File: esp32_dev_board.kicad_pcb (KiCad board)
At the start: 4 copper layers, 0 parts

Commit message: Start layout.
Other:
- board outline added: 100 x 40 mm
- rule via_min_size: 0.4 -> 0.45
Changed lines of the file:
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@@
   (general
     (thickness 1.6)
-    (drawings 0)
+    (drawings 8)
     (tracks 0)
     (zones 0)
@@
     (0 F.Cu signal)
     (1 In1.Cu power)
-    (2 In2.Cu signal)
+    (2 In2.Cu power)
     (31 B.Cu signal)
-    (33 F.Adhes user)
+    (34 B.Paste user)
     (35 F.Paste user)
+    (36 B.SilkS user)
     (37 F.SilkS user)
+    (38 B.Mask user)
     (39 F.Mask user)
     (40 Dwgs.User user)
@@
     (46 B.CrtYd user)
     (47 F.CrtYd user)
+    (48 B.Fab user)
     (49 F.Fab user)
   )
@@
     (via_size 0.8)
     (via_drill 0.4)
-    (via_min_size 0.4)
+    (via_min_size 0.45)
     (via_min_drill 0.3)
     (uvia_size 0.3)
@@
     (uvia_drill 0.1)
   )
+  (gr_line (start 80.2 80.2) (end 80.2 119.8) (layer Margin) (width 0.15))
+  (gr_line (start 179.8 80.2) (end 80.2 80.2) (layer Margin) (width 0.15))
+  (gr_line (start 179.8 119.8) (end 179.8 80.2) (layer Margin) (width 0.15))
+  (gr_line (start 80.2 119.8) (end 179.8 119.8) (layer Margin) (width 0.15))
+  (gr_line (start 80 80) (end 80 120) (layer Edge.Cuts) (width 0.05))
+  (gr_line (start 180 80) (end 80 80) (layer Edge.Cuts) (width 0.05))
+  (gr_line (start 180 120) (end 180 80) (layer Edge.Cuts) (width 0.05))
+  (gr_line (start 80 120) (end 180 120) (layer Edge.Cuts) (width 0.05))
 )

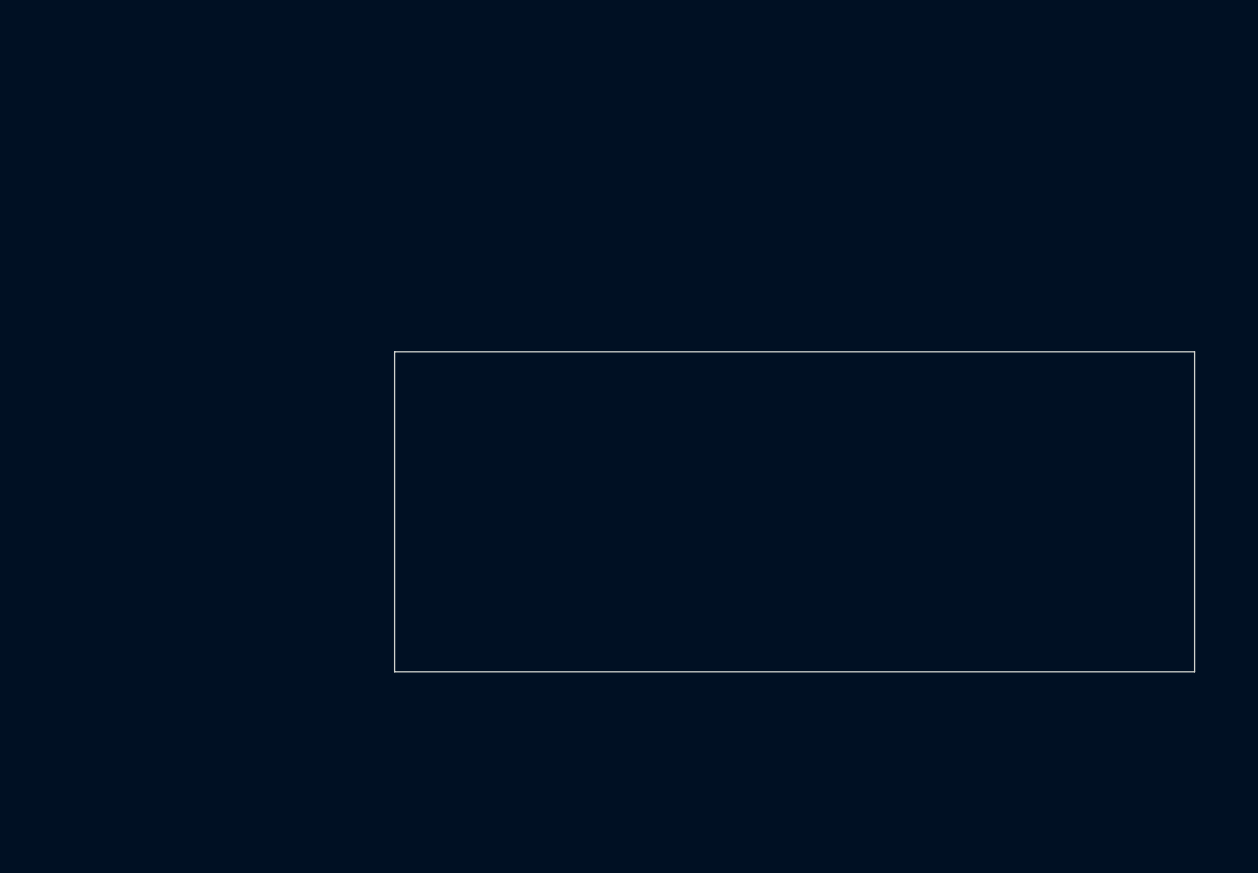
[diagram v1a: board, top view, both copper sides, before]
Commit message: Fix wrong footprint on GigaDevice part (correct in library though).
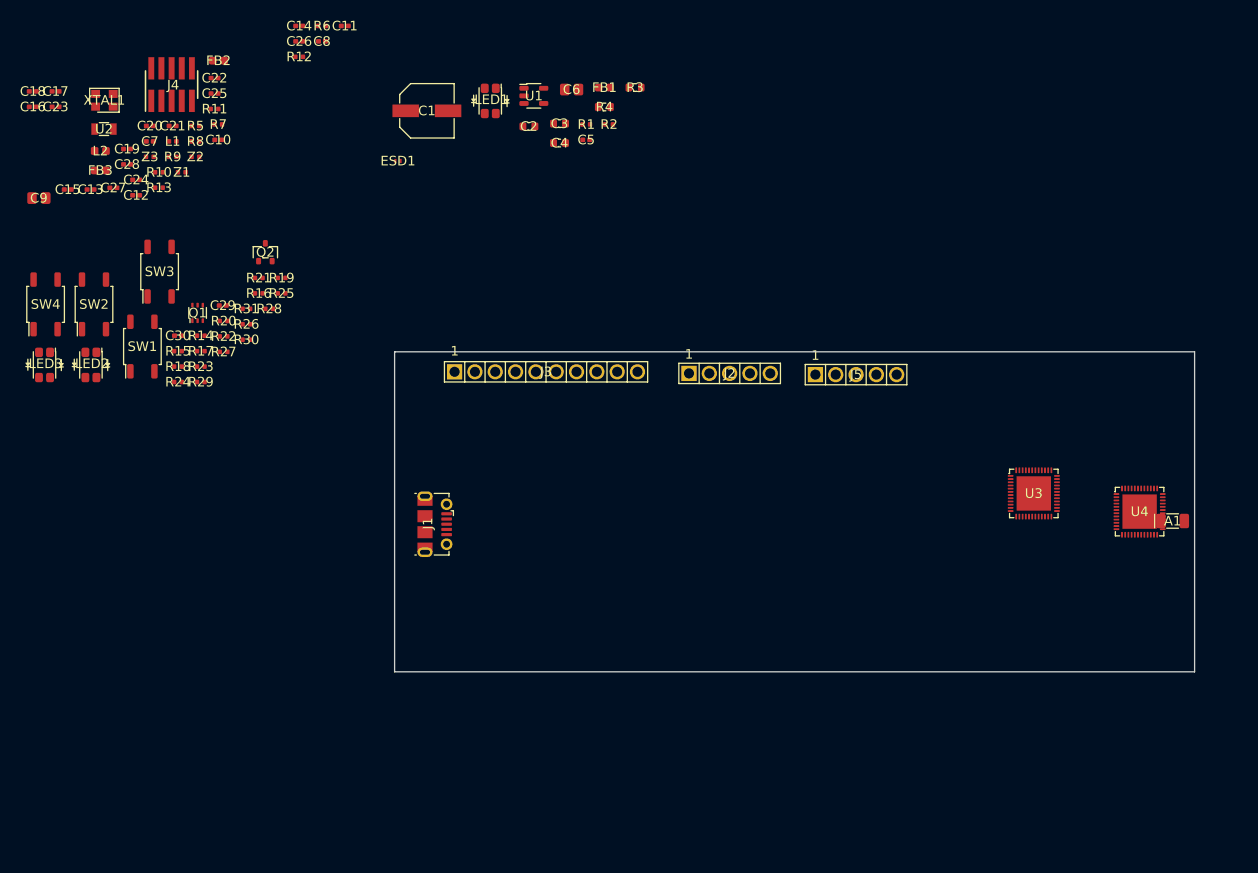
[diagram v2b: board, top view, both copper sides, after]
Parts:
- added A1: WE-7488930245, footprints:WE-7488930245_ANTC320X160X140L50N, F.Cu at (177.2, 101.2)
- added C1: WE-865080245009, footprints_generic:WE-86508xx450xx_CAPAE660X770D730L255X65N, F.Cu at (84.0, 49.9)
- added C10: CAP-EIA0402, footprints_generic:CAPC100X50X55L30N, F.Cu at (58.0, 53.5)
- added C11: CAP-EIA0402, footprints_generic:CAPC100X50X55L30N, F.Cu at (73.8, 39.3)
- added C12: CAP-EIA0402, footprints_generic:CAPC100X50X55L30N, F.Cu at (47.7, 60.4)
- added C13: CAP-EIA0402, footprints_generic:CAPC100X50X55L30N, F.Cu at (42.0, 59.7)
- added C14: CAP-EIA0402, footprints_generic:CAPC100X50X55L30N, F.Cu at (68.1, 39.3)
- added C15: CAP-EIA0402, footprints_generic:CAPC100X50X55L30N, F.Cu at (39.1, 59.7)
- added C16: CAP-EIA0402, footprints_generic:CAPC100X50X55L30N, F.Cu at (34.8, 49.4)
- added C17: CAP-EIA0402, footprints_generic:CAPC100X50X55L30N, F.Cu at (37.6, 47.4)
- added C18: CAP-EIA0402, footprints_generic:CAPC100X50X55L30N, F.Cu at (34.8, 47.4)
- added C19: CAP-EIA0402, footprints_generic:CAPC100X50X55L30N, F.Cu at (46.6, 54.6)
- added C2: CAP-EIA0603, footprints_generic:CAPC160X80X95L35N, F.Cu at (96.8, 51.8)
- added C20: CAP-EIA0402, footprints_generic:CAPC100X50X55L30N, F.Cu at (49.4, 51.8)
- added C21: CAP-EIA0402, footprints_generic:CAPC100X50X55L30N, F.Cu at (52.3, 51.8)
- added C22: CAP-EIA0402, footprints_generic:CAPC100X50X55L30N, F.Cu at (57.5, 45.8)
- added C23: CAP-EIA0402, footprints_generic:CAPC100X50X55L30N, F.Cu at (37.6, 49.4)
- added C24: CAP-EIA0402, footprints_generic:CAPC100X50X55L30N, F.Cu at (47.7, 58.5)
- added C25: CAP-EIA0402, footprints_generic:CAPC100X50X55L30N, F.Cu at (57.5, 47.7)
- added C26: CAP-EIA0402, footprints_generic:CAPC100X50X55L30N, F.Cu at (68.1, 41.2)
- added C27: CAP-EIA0402, footprints_generic:CAPC100X50X55L30N, F.Cu at (44.8, 59.5)
- added C28: CAP-EIA0402, footprints_generic:CAPC100X50X55L30N, F.Cu at (46.6, 56.6)
- added C29: CAP-EIA0402, footprints_generic:CAPC100X50X55L30N, F.Cu at (58.5, 74.2)
- added C3: CAP-EIA0603, footprints_generic:CAPC160X80X95L35N, F.Cu at (100.6, 51.5)
- added C30: CAP-EIA0402, footprints_generic:CAPC100X50X55L30N, F.Cu at (52.9, 78.0)
- added C4: CAP-EIA0603, footprints_generic:CAPC160X80X95L35N, F.Cu at (100.6, 53.9)
- added C5: CAP-EIA0402, footprints_generic:CAPC100X50X55L30N, F.Cu at (104.0, 53.5)
- added C6: CAP-EIA0805, footprints_generic:CAPC200X125X110L50N, F.Cu at (102.1, 47.2)
- added C7: CAP-EIA0402, footprints_generic:CAPC100X50X55L30N, F.Cu at (49.4, 53.7)
- added C8: CAP-EIA0402, footprints_generic:CAPC100X50X55L30N, F.Cu at (70.9, 41.2)
- added C9: CAP-EIA0805, footprints_generic:CAPC200X125X110L50N, F.Cu at (35.5, 60.8)
- added ESD1: TI-TPD1E10B09DPYT, footprints:TI-TPD1E10B09DPYT_DIODFN2_100X60X45L25X50N, F.Cu at (80.4, 56.1)
- added FB1: FB-EIA0603, footprints_generic:BEADC160X80X95L40N, F.Cu at (106.2, 47.0)
- added FB2: FB-EIA0603, footprints_generic:BEADC160X80X95L40N, F.Cu at (58.0, 43.6)
- added FB3: FB-EIA0603, footprints_generic:BEADC160X80X95L40N, F.Cu at (43.2, 57.3)
- added J1: Molex-1050170001, footprints:Molex-1050170001, F.Cu at (82.3, 101.5)
- added J2: WE-61300511121, footprints:WE-61300511121_HDRV5W79P254_5X1_1270X254H854, F.Cu at (116.8, 82.7)
- added J3: WE-61301011121, footprints:WE-61301011121_HDRV10W64P254_10X1_2540X254X884N, F.Cu at (87.5, 82.5)
- added J4: Samtec-FTSH-105-01-F-DV-K-TR, footprints:Samtec_FTSH-105-01-F-DV-K-TR, F.Cu at (52.1, 46.6)
- added J5: WE-61300511121, footprints:WE-61300511121_HDRV5W79P254_5X1_1270X254H854, F.Cu at (132.6, 82.8)
- added L1: IND-EIA0402, footprints_generic:INDC100X50X55L25N, F.Cu at (52.3, 53.7)
- added L2: IND-EIA0603, footprints_generic:INDC160X80X95L40N, F.Cu at (43.2, 54.9)
- added LED1: LiteOn-LTST-C155KGJRKT, footprints:LiteOn-LTST-C155_LEDCAV4P138_270X320X110L50X90N, F.Cu at (92.0, 48.6)
- added LED2: LiteOn-LTST-C155KGJRKT, footprints:LiteOn-LTST-C155_LEDCAV4P138_270X320X110L50X90N, F.Cu at (42.0, 81.6)
- added LED3: LiteOn-LTST-C155KGJRKT, footprints:LiteOn-LTST-C155_LEDCAV4P138_270X320X110L50X90N, F.Cu at (36.2, 81.6)
- added Q1: ON-Semi_MUN5211DW1T1G, footprints:ON-Semi-MUN5211DW1T1G_SOT23-6P65_210X110L36X20L, F.Cu at (55.4, 75.1)
- added Q2: ON-Semi_BC858CLT1G, footprints:ON-Semi-BC858CLT1G_SOT23-3P85_237X111L42X43N, F.Cu at (63.8, 67.6)
- added R1: RES-EIA0402, footprints_generic:RESC100X50X40L25NN, F.Cu at (104.0, 51.6)
- added R10: RES-EIA0402, footprints_generic:RESC100X50X40L25NN, F.Cu at (50.5, 57.6)
- added R11: RES-EIA0402, footprints_generic:RESC100X50X40L25NN, F.Cu at (57.5, 49.6)
- added R12: RES-EIA0402, footprints_generic:RESC100X50X40L25NN, F.Cu at (68.1, 43.1)
- added R13: RES-EIA0402, footprints_generic:RESC100X50X40L25NN, F.Cu at (50.5, 59.5)
- added R14: RES-EIA0402, footprints_generic:RESC100X50X40L25NN, F.Cu at (55.8, 78.0)
- added R15: RES-EIA0402, footprints_generic:RESC100X50X40L25NN, F.Cu at (52.9, 79.9)
- added R16: RES-EIA0402, footprints_generic:RESC100X50X40L25NN, F.Cu at (63.0, 72.7)
- added R17: RES-EIA0402, footprints_generic:RESC100X50X40L25NN, F.Cu at (55.8, 79.9)
- added R18: RES-EIA0402, footprints_generic:RESC100X50X40L25NN, F.Cu at (52.9, 81.8)
- added R19: RES-EIA0402, footprints_generic:RESC100X50X40L25NN, F.Cu at (65.9, 70.8)
- added R2: RES-EIA0402, footprints_generic:RESC100X50X40L25NN, F.Cu at (106.8, 51.6)
- added R20: RES-EIA0402, footprints_generic:RESC100X50X40L25NN, F.Cu at (58.6, 76.1)
- added R21: RES-EIA0402, footprints_generic:RESC100X50X40L25NN, F.Cu at (63.0, 70.8)
- added R22: RES-EIA0402, footprints_generic:RESC100X50X40L25NN, F.Cu at (58.6, 78.1)
- added R23: RES-EIA0402, footprints_generic:RESC100X50X40L25NN, F.Cu at (55.8, 81.8)
- added R24: RES-EIA0402, footprints_generic:RESC100X50X40L25NN, F.Cu at (52.9, 83.8)
- added R25: RES-EIA0402, footprints_generic:RESC100X50X40L25NN, F.Cu at (65.9, 72.7)
- added R26: RES-EIA0402, footprints_generic:RESC100X50X40L25NN, F.Cu at (61.5, 76.6)
- added R27: RES-EIA0402, footprints_generic:RESC100X50X40L25NN, F.Cu at (58.6, 80.0)
- added R28: RES-EIA0402, footprints_generic:RESC100X50X40L25NN, F.Cu at (64.3, 74.6)
- added R29: RES-EIA0402, footprints_generic:RESC100X50X40L25NN, F.Cu at (55.8, 83.8)
- added R3: RES-EIA0603, footprints_generic:RESC160X85X55L30N, F.Cu at (110.1, 47.0)
- added R30: RES-EIA0402, footprints_generic:RESC100X50X40L25NN, F.Cu at (61.5, 78.5)
- added R31: RES-EIA0402, footprints_generic:RESC100X50X40L25NN, F.Cu at (61.5, 74.6)
- added R4: RES-EIA0603, footprints_generic:RESC160X85X55L30N, F.Cu at (106.2, 49.4)
- added R5: RES-EIA0402, footprints_generic:RESC100X50X40L25NN, F.Cu at (55.1, 51.8)
- added R6: RES-EIA0402, footprints_generic:RESC100X50X40L25NN, F.Cu at (70.9, 39.3)
- added R7: RES-EIA0402, footprints_generic:RESC100X50X40L25NN, F.Cu at (58.0, 51.6)
- added R8: RES-EIA0402, footprints_generic:RESC100X50X40L25NN, F.Cu at (55.1, 53.7)
- added R9: RES-EIA0402, footprints_generic:RESC100X50X40L25NN, F.Cu at (52.3, 55.6)
- added SW1: WE-430181038816, footprints:WE-430181038816_SWSOFL4P150_450X750X380L150X70N, F.Cu at (48.5, 79.3)
- added SW2: WE-430181038816, footprints:WE-430181038816_SWSOFL4P150_450X750X380L150X70N, F.Cu at (42.4, 74.1)
- added SW3: WE-430181038816, footprints:WE-430181038816_SWSOFL4P150_450X750X380L150X70N, F.Cu at (50.6, 70.0)
- added SW4: WE-430181038816, footprints:WE-430181038816_SWSOFL4P150_450X750X380L150X70N, F.Cu at (36.4, 74.1)
- added U1: TI-TLV75533PDBVR, footprints:TI-TLV755_SOT23-5P95_280X145L45X40N, F.Cu at (97.4, 48.0)
- added U2: RaltronElectronics-RT3215-32.768-6-TR, footprints:RaltronElectronics-RT3215_XTALDFN2_320X150X90L65X130N, F.Cu at (43.7, 52.2)
- added U3: Espressif_ESP32-D0WDQ6-V3, footprints:Espressif-ESP32_QFN49P40_600X600X90L40X20T430N, F.Cu at (159.9, 97.7)
- added U4: GigaDevice-GD25Q64CSIGR, footprints:Espressif-ESP32_QFN49P40_600X600X90L40X20T430N, F.Cu at (173.1, 100.0)
- added XTAL1: RaltronElectronics-RH100-40.000-9-F-1010-EXT-TR, footprints:RaltronElectronics-RH100_XTALDFN4_250X320X80L90X100N, F.Cu at (43.7, 48.6)
- added Z1: Z-EIA0402, footprints_generic:RESC100X50X40L25NN, F.Cu at (53.4, 57.6)
- added Z2: Z-EIA0402, footprints_generic:RESC100X50X40L25NN, F.Cu at (55.1, 55.6)
- added Z3: Z-EIA0402, footprints_generic:RESC100X50X40L25NN, F.Cu at (49.4, 55.6)

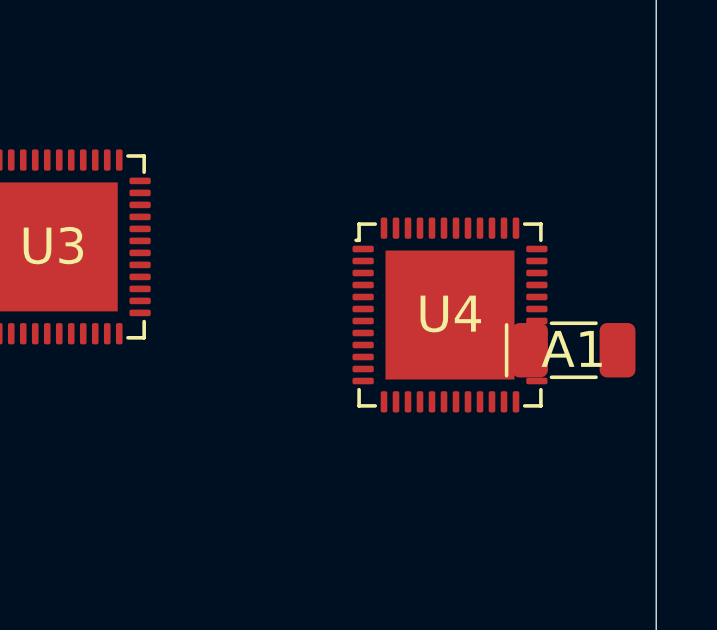
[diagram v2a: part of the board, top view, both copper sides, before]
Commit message: Update J4 footprint after removing leading zeros in pad names.
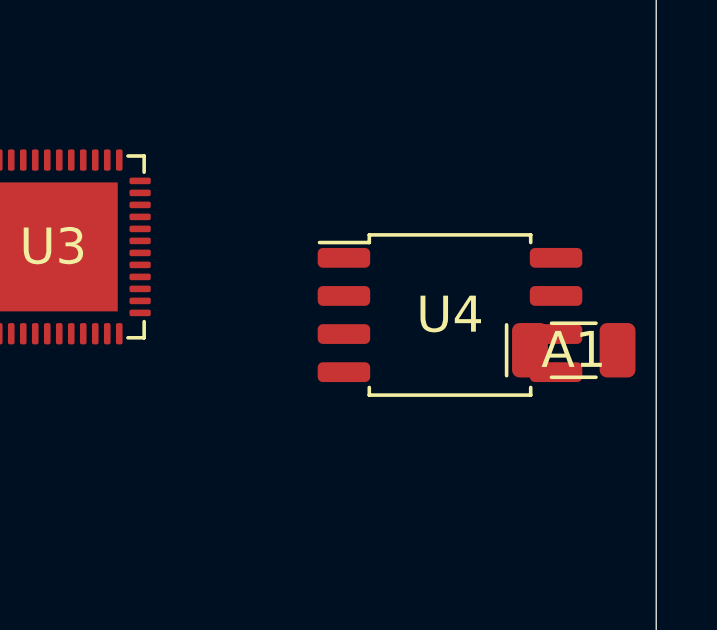
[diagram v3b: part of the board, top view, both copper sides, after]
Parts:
- U4: footprint footprints:Espressif-ESP32_QFN49P40_600X600X90L40X20T430N -> footprints:GigaDevice-GD25Q64CS_SOIC8P127_523X790X216L67X41N

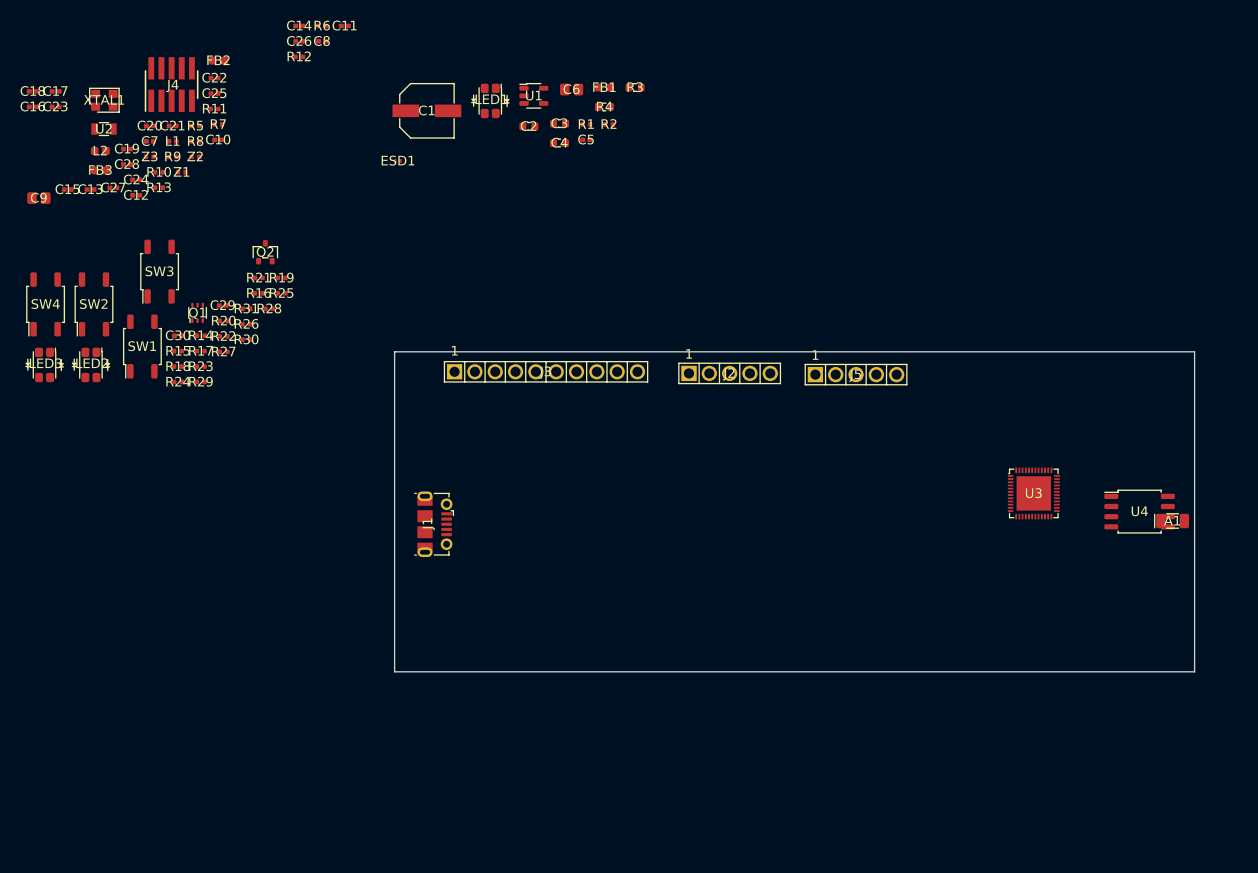
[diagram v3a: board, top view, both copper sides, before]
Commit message: Update power symbols after change to pin names; annotate.
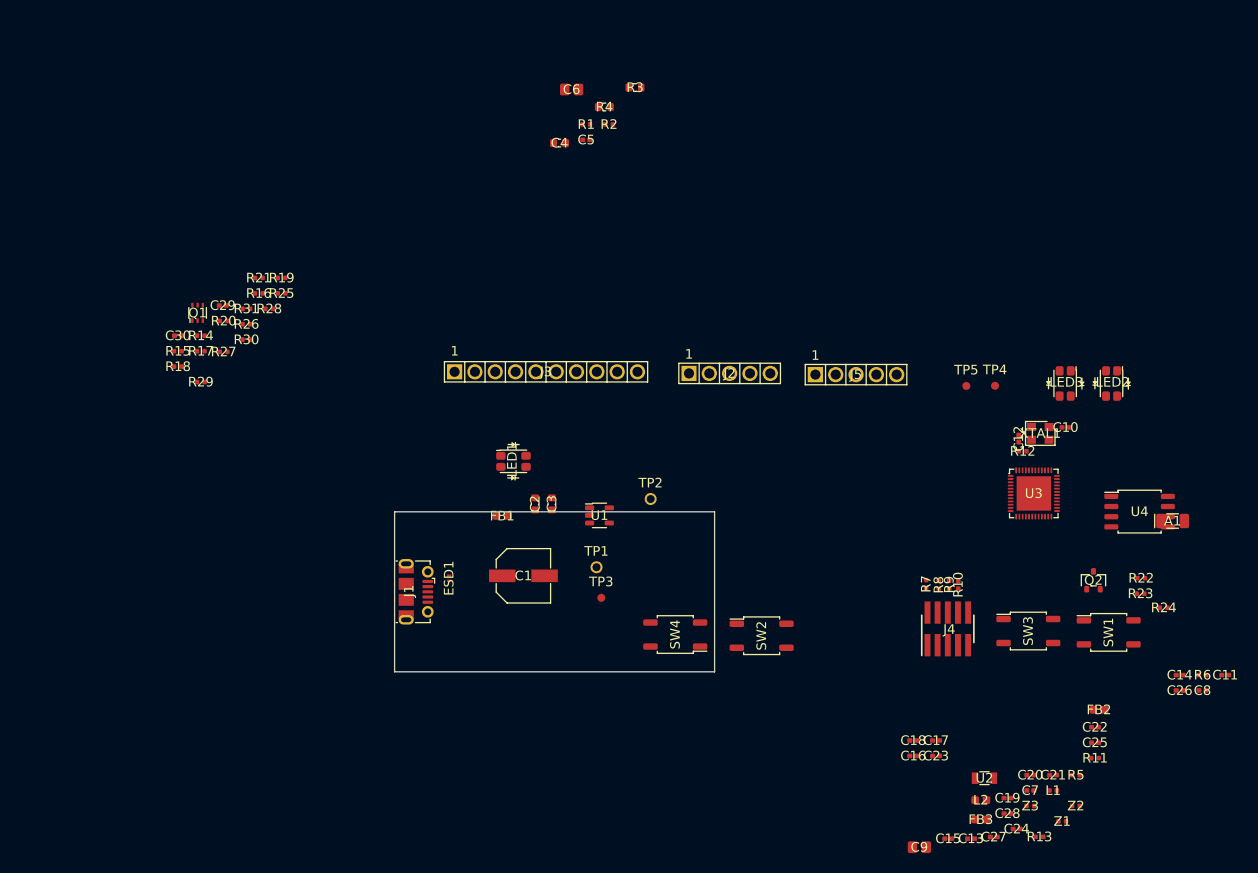
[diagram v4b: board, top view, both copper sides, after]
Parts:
- added TP1: Test-Point-THT, footprints_generic:TestPoint-THT_C150H100, F.Cu at (105.2, 106.9)
- added TP2: Test-Point-THT, footprints_generic:TestPoint-THT_C150H100, F.Cu at (112.0, 98.4)
- added TP3: Test-Point-SMT, footprints_generic:TestPoint-SMT_C100, F.Cu at (105.8, 110.8)
- added TP4: Test-Point-SMT, footprints_generic:TestPoint-SMT_C100, F.Cu at (155.1, 84.2)
- added TP5: Test-Point-SMT, footprints_generic:TestPoint-SMT_C100, F.Cu at (151.5, 84.3)
- moved C11 136.7 mm to (183.8, 120.4)
- moved C13 136.7 mm to (152.1, 140.9)
- moved C15 136.7 mm to (149.2, 140.9)
- moved C16 136.7 mm to (144.8, 130.5)
- moved C17 136.7 mm to (147.7, 128.6)
- moved C18 136.7 mm to (144.8, 128.6)
- moved C19 136.7 mm to (156.6, 135.8)
- moved C20 136.7 mm to (159.5, 132.9)
- moved C21 136.7 mm to (162.3, 132.9)
- moved C22 136.7 mm to (167.6, 126.9)
- moved C23 136.7 mm to (147.7, 130.5)
- moved C24 136.7 mm to (157.8, 139.6)
- moved C25 136.7 mm to (167.6, 128.9)
- moved C27 136.7 mm to (154.9, 140.6)
- moved C28 136.7 mm to (156.6, 137.7)
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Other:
- board size 100 x 40 mm -> 40 x 20 mm

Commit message: Mid-way through placement.
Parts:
- moved R24 80.0 mm to (96.1, 111.7)
- moved U4 70.6 mm to (103.0, 108.5)
- moved R1 64.6 mm to (95.2, 115.6), turned to 180 degrees
- moved R3 59.7 mm to (86.2, 101.7)
- moved R2 56.4 mm to (88.4, 104.9), turned to 270 degrees
- moved R4 53.1 mm to (94.0, 101.1)
- moved C6 52.8 mm to (92.8, 99.2)
- moved C5 52.8 mm to (90.0, 104.4)
- moved A1 52.8 mm to (127.5, 118.7)
- moved U3 50.5 mm to (112.1, 113.9), turned to 180 degrees
- moved L1 47.9 mm to (118.4, 115.7)
- moved C4 47.6 mm to (87.2, 99.6), turned to 180 degrees
- moved Z1 47.3 mm to (120.5, 118.9), turned to 180 degrees
- moved Z2 46.3 mm to (122.4, 118.9), turned to 180 degrees
- moved C13 43.4 mm to (117.0, 115.3), turned to 90 degrees
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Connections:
- C1 pad 1: +3V3 -> 5V
- C11 pad 1: +3V3 -> 3V3A
- C14 pad 1: +3V3 -> 3V3A
- C15 pad 1: +3V3 -> 3V3A
- C16 pad 1: +3V3 -> 3V3A
- C17 pad 1: +3V3 -> 3V3A
- C2 pad 1: +3V3 -> 5V
- C21 pad 1: +3V3 -> 3V3A
- C22 pad 1: +3V3 -> 3V3A
- C24 pad 1: +3V3 -> 3V3
- C25 pad 1: +3V3 -> 3V3
- C26 pad 1: +3V3 -> 3V3D
- C28 pad 1: +3V3 -> 3V3D
- C29 pad 1: +3V3 -> 3V3
- C3 pad 1: +3V3 -> 5V
- C4 pad 1: +3V3 -> 5V
- C4 pad 2: GND -> PSU
- C5 pad 2: GND -> PSU
- C6 pad 2: GND -> PSU
- C9 pad 1: +3V3 -> 3V3A
- FB1 pad 2: +3V3 -> 5V
- FB2 pad 1: +3V3 -> 3V3A
- FB2 pad 2: +3V3 -> 3V3
- FB3 pad 1: +3V3 -> 3V3
- FB3 pad 2: +3V3 -> 3V3D
- J4 pad 1: +3V3 -> 3V3
- L2 pad 1: +3V3 -> 3V3A
- Q2 pad 2: +3V3 -> 3V3
- R1 pad 2: +3V3 -> 5V
- R14 pad 1: +3V3 -> 3V3
- R15 pad 1: +3V3 -> 3V3
- R16 pad 1: +3V3 -> 3V3
- R17 pad 1: +3V3 -> 3V3
- R18 pad 1: +3V3 -> 3V3
- R2 pad 2: +3V3 -> 5V
- R22 pad 1: +3V3 -> 3V3
- R27 pad 1: +3V3 -> 3V3
- R3 pad 2: GND -> PSU
- R30 pad 1: +3V3 -> 3V3
- R31 pad 1: +3V3 -> 3V3
- R4 pad 2: +3V3 -> 3V3
- TP1 pad 1: +3V3 -> 5V
- TP3 pad 1: +3V3 -> 3V3
- TP4 pad 1: +3V3 -> 3V3A
- TP5 pad 1: +3V3 -> 3V3D
- U1 pad 1: +3V3 -> 5V
- U1 pad 2: GND -> PSU
- U3 pad 1: +3V3 -> 3V3A
- U3 pad 19: +3V3 -> 3V3D
- U3 pad 37: +3V3 -> 3V3D
- U3 pad 43: +3V3 -> 3V3A
- U3 pad 46: +3V3 -> 3V3A
- U4 pad 8: +3V3 -> 3V3
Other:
- board size 40 x 20 mm -> 50 x 25 mm

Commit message: Update placement.
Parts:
- moved LED2 103.7 mm to (75.7, 127.9), turned to 180 degrees
- moved R14 97.5 mm to (131.6, 139.3)
- moved R15 97.5 mm to (128.7, 141.2)
- moved R16 97.5 mm to (138.8, 134.0)
- moved R17 97.5 mm to (131.6, 141.2)
- moved R28 80.5 mm to (119.4, 133.3)
- moved R29 80.0 mm to (119.4, 132.2)
- moved SW1 79.6 mm to (89.8, 109.9), turned to 90 degrees
- moved R22 78.3 mm to (95.1, 111.3), turned to 180 degrees
- moved R23 78.2 mm to (95.1, 112.3)
- moved R26 77.0 mm to (113.6, 133.2)
- moved R25 76.2 mm to (113.6, 132.1)
- moved Q2 71.2 mm to (96.2, 108.9), turned to 270 degrees
- moved C8 70.7 mm to (113.3, 101.8)
- moved SW3 69.9 mm to (89.3, 116.9), turned to 90 degrees
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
